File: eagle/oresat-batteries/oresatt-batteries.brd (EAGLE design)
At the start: 94 x 93.5 mm, 22 parts, among them U1 TCAN330

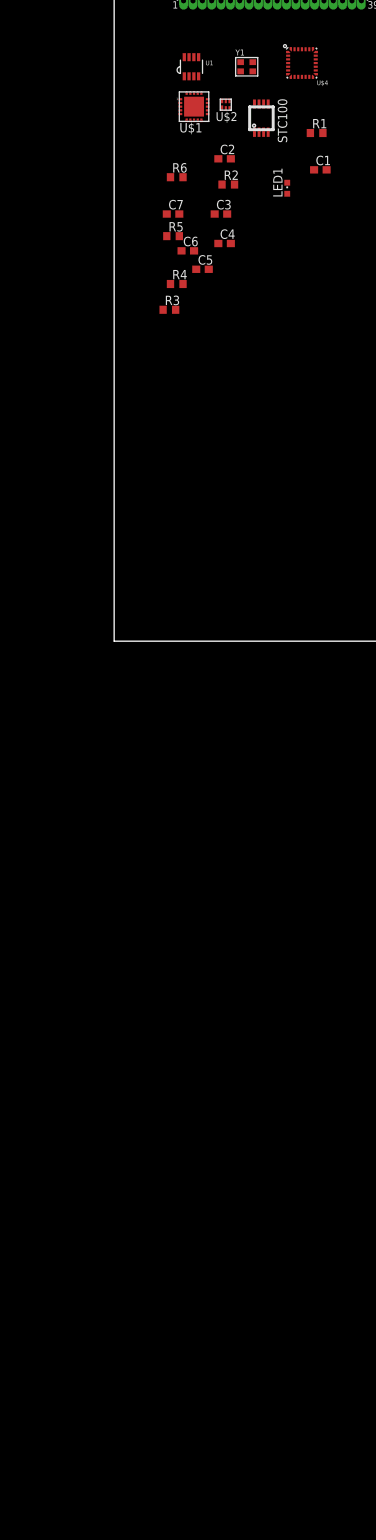
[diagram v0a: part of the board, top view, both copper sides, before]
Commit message: Finished first draft of schematics.
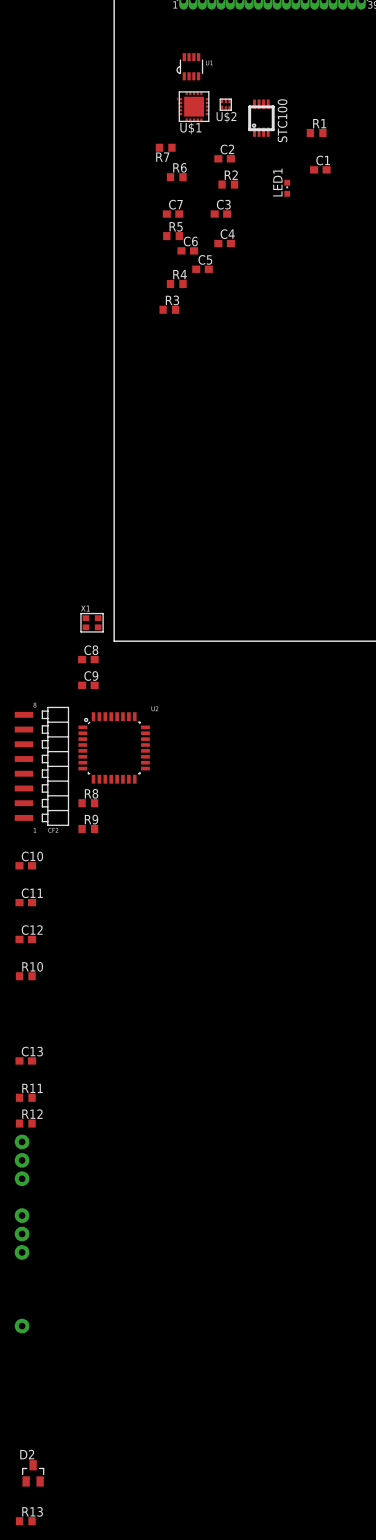
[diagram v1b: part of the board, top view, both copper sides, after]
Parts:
- removed Y1: (no value), low-gain-radio:CRYSTAL_2.5X2
- added C10, C11, C12, C13: 100n, rcl:C0603
- added C8, C9: 20p, rcl:C0603
- added CF2: 2MM-RA-1X8, oresat-batteries:CF-2MM-RA-1X8-PRECIDIP-831
- added D2: BAS40, diode:SOT23
- added R10, R12: 10k, rcl:R0603
- added R11, R7: (no value), rcl:R0603
- added R13: DNP/0, rcl:R0603
- added R8, R9: 4.7k, rcl:R0603
- added U$10, U$11, U$15, U$6, U$7, U$9: TP, oresat-batteries:2MM_TP
- added U2: STM32F042K6, oresat-batteries:QFP32-7X7
- added X1: 16MHz, low-gain-radio:CRYSTAL_2.5X2
- R1: value Sense -> THERMISTER
- R3: value Sense -> .01-.05
- R4: value Sense -> 200k .1%
- U$4: value STM32F042G -> TP; device oresat-batteries:UFQFPN-28 -> oresat-batteries:2MM_TP
- moved U$4 151.3 mm to (-12.5, -68.0)
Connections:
- net N$1 renamed ADP_THR
- net N$10 renamed BQVMIN
- net N$2 renamed LEDNP
- net N$3 renamed ADP_LED
- net N$9 renamed STC_VIN
- removed net N$5: C5.1, CF1.P$3, U$1.6, U$1.7, U$1.8
- removed net N$6: C4.1
- removed net N$8: R3.2
- removed net VCC: U1.3
- removed net VDD: U$4.17
- removed net VDDA: U$4.5
- removed net VDDIO2: U$4.18
- removed net VSS: U$4.16
- new net ADP_CBP: C4.1, U$1.19
- new net BQBAT: C1.1, R7.1, U$2.5
- new net CAN_EN: U1.5, U2.20
- new net CAN_LSTN: U1.8, U2.19
- new net CAN_RX: U1.4, U2.21
- new net CAN_TX: U1.1, U2.22
- new net ISO_S: C3.1, CF1.P$2, U$1.10, U$1.11, U$1.9
- new net N$1: C7.2, R11.1, U$5.7
- new net N$2: R12.2, U2.31
- new net N$3: R10.1, R13.2, U$5.1
- new net N$31: CF2.3, U2.4
- new net OSC_IN: C8.1, U2.2, X1.1
- new net OSC_OUT: C9.1, U2.3, X1.3
- new net SCL: R8.1, U$1.1, U$5.4, U2.29
- new net SDA: R9.1, U$1.17, U$5.3, U2.30
- new net STC_CG: R3.2, U$5.6
- new net STC_IO: R13.1, U2.28
- new net STM_DEBUG: CF2.8, U2.10
- new net SWCLK: CF2.4, U2.24
- new net SWDIO: CF2.5, U2.23
- new net USART2_RX: CF2.7, U2.9
- new net USART2_TX: CF2.6, U2.8
- new net VSOLAR: C5.1, CF1.P$3, R8.2, R9.2, U$1.6, U$1.7, U$1.8
- net GND: now also C10.2, C11.2, C12.2, C13.2, C8.2, C9.2, CF2.1, R12.1, U2.16, U2.32, X1.2, X1.4
- net N$4: now also D2.3; no longer C3.1, U$1.10, U$1.11, U$1.9
- net VBAT+: now also C10.1, C11.1, C12.1, C13.1, CF2.2, D2.1, R11.2, R7.2, U1.3, U2.1, U2.17, U2.5; no longer C1.1, C7.2, U$2.5, U$5.7

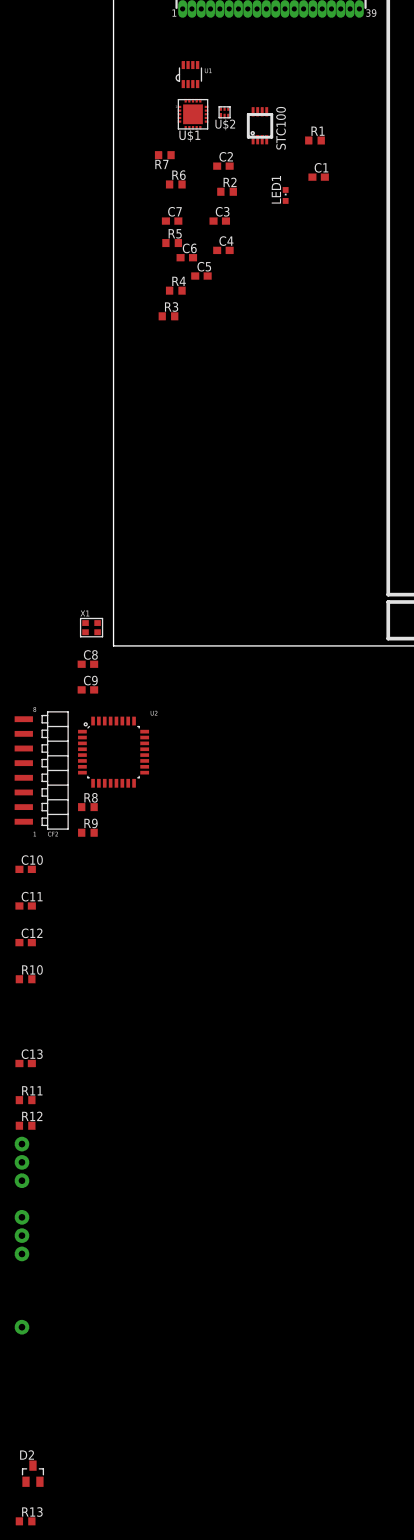
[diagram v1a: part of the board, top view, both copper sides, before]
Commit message: Minor clean up, added debug board, serial marker
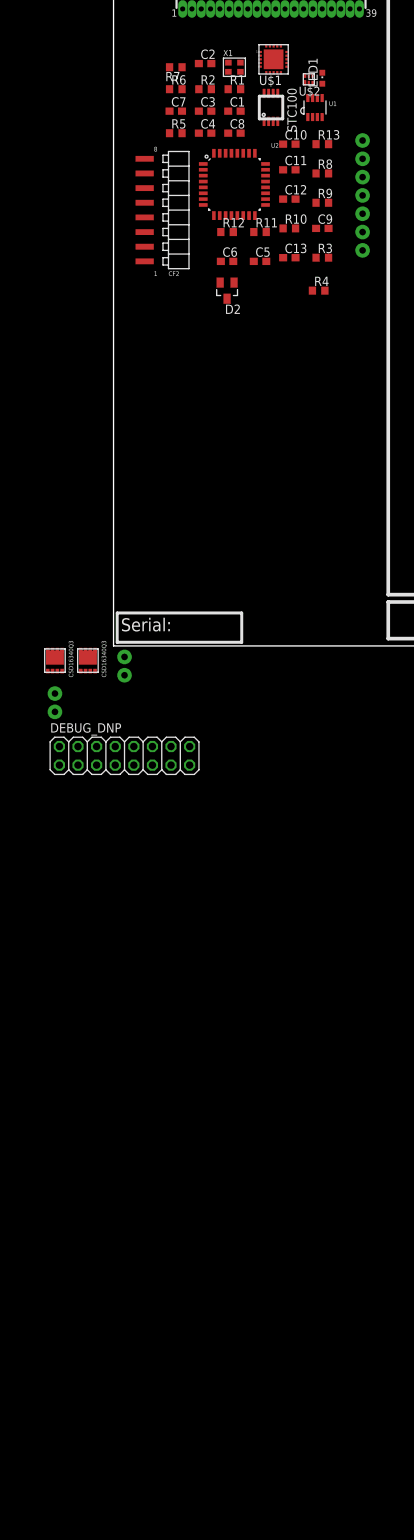
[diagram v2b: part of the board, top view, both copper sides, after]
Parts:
- added DEBUG_DNP: (no value), pinhead:2X08
- added U$12, U$16, U$17, U$8: TP, oresat-batteries:2MM_TP
- added U$13, U$14: CSD16340Q3, oresat-batteries:Q3
- R8, R9: value 4.7k -> 1.6k
- moved R13 192.3 mm to (28.5, 68.5)
- moved D2 163.7 mm to (15.5, 48.5), turned to 180 degrees
- moved U$15 154.2 mm to (34.0, 54.0)
- moved U$10 147.0 mm to (34.0, 59.0)
- moved U$11 147.0 mm to (34.0, 56.5)
- moved U$9 147.0 mm to (34.0, 61.5)
- moved U$4 144.7 mm to (34.0, 69.0)
- moved U$6 144.7 mm to (34.0, 66.5)
- moved U$7 144.7 mm to (34.0, 64.0)
- moved R12 125.1 mm to (15.5, 56.5)
- moved R11 122.7 mm to (20.0, 56.5)
- moved C13 115.7 mm to (24.0, 53.0)
- moved R10 108.6 mm to (24.0, 57.0)
- moved C12 107.7 mm to (24.0, 61.0)
- moved C11 106.8 mm to (24.0, 65.0)
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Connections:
- removed net VBAT+: C10.1, C11.1, C12.1, C13.1, C2.1, CF2.2, D2.1, R11.2, R5.1, R7.2, U$1.12, U$1.13, U$1.14, U$1.4, U1.3, U2.1, U2.17, U2.5
- new net N$10: U$14.P$4, U$2.3
- new net N$11: U$13.P$4, U$2.2
- new net N$5: CF1.P$4, DEBUG_DNP.13, DEBUG_DNP.14, U1.7
- new net N$6: CF1.P$5, DEBUG_DNP.11, DEBUG_DNP.12, U1.6
- new net N$9: U$13.P$5, U$13.P$6, U$13.P$7, U$13.P$8, U$13.P$9, U$14.P$5, U$14.P$6, U$14.P$7, U$14.P$8, U$14.P$9
- new net VBATT+: C10.1, C11.1, C12.1, C13.1, C2.1, CF2.2, D2.1, DEBUG_DNP.1, DEBUG_DNP.2, R11.2, R5.1, R7.2, R8.2, R9.2, U$1.12, U$1.13, U$1.14, U$1.4, U1.3, U2.1, U2.17, U2.5
- net GND: now also DEBUG_DNP.15, DEBUG_DNP.16, U$13.P$1, U$13.P$2, U$13.P$3
- net SCL: now also R9.1; no longer R8.1
- net SDA: now also R8.1; no longer R9.1
- net STC_CG: now also U$14.P$1, U$14.P$2, U$14.P$3
- net USART2_RX: now also DEBUG_DNP.5, DEBUG_DNP.6
- net USART2_TX: now also DEBUG_DNP.3, DEBUG_DNP.4
- net VSOLAR: now also DEBUG_DNP.7, DEBUG_DNP.8; no longer R8.2, R9.2
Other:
- board text added: "Serial:"

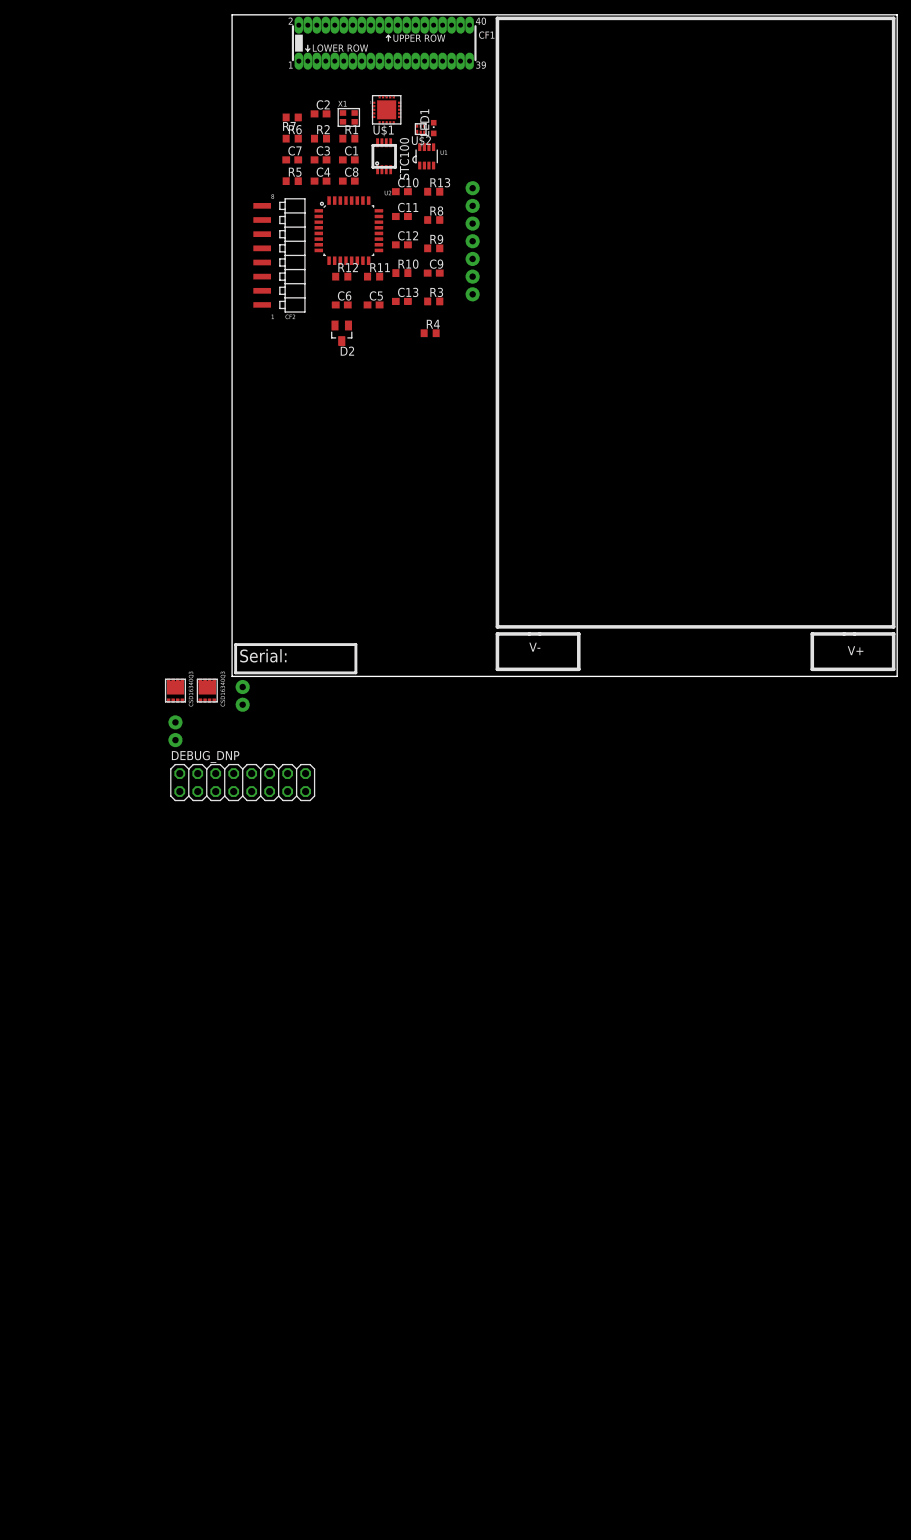
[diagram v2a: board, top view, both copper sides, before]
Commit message: Added, resistive heater, half of shutdown circuitry, connected DIG_IOx and SYS_EN pins.
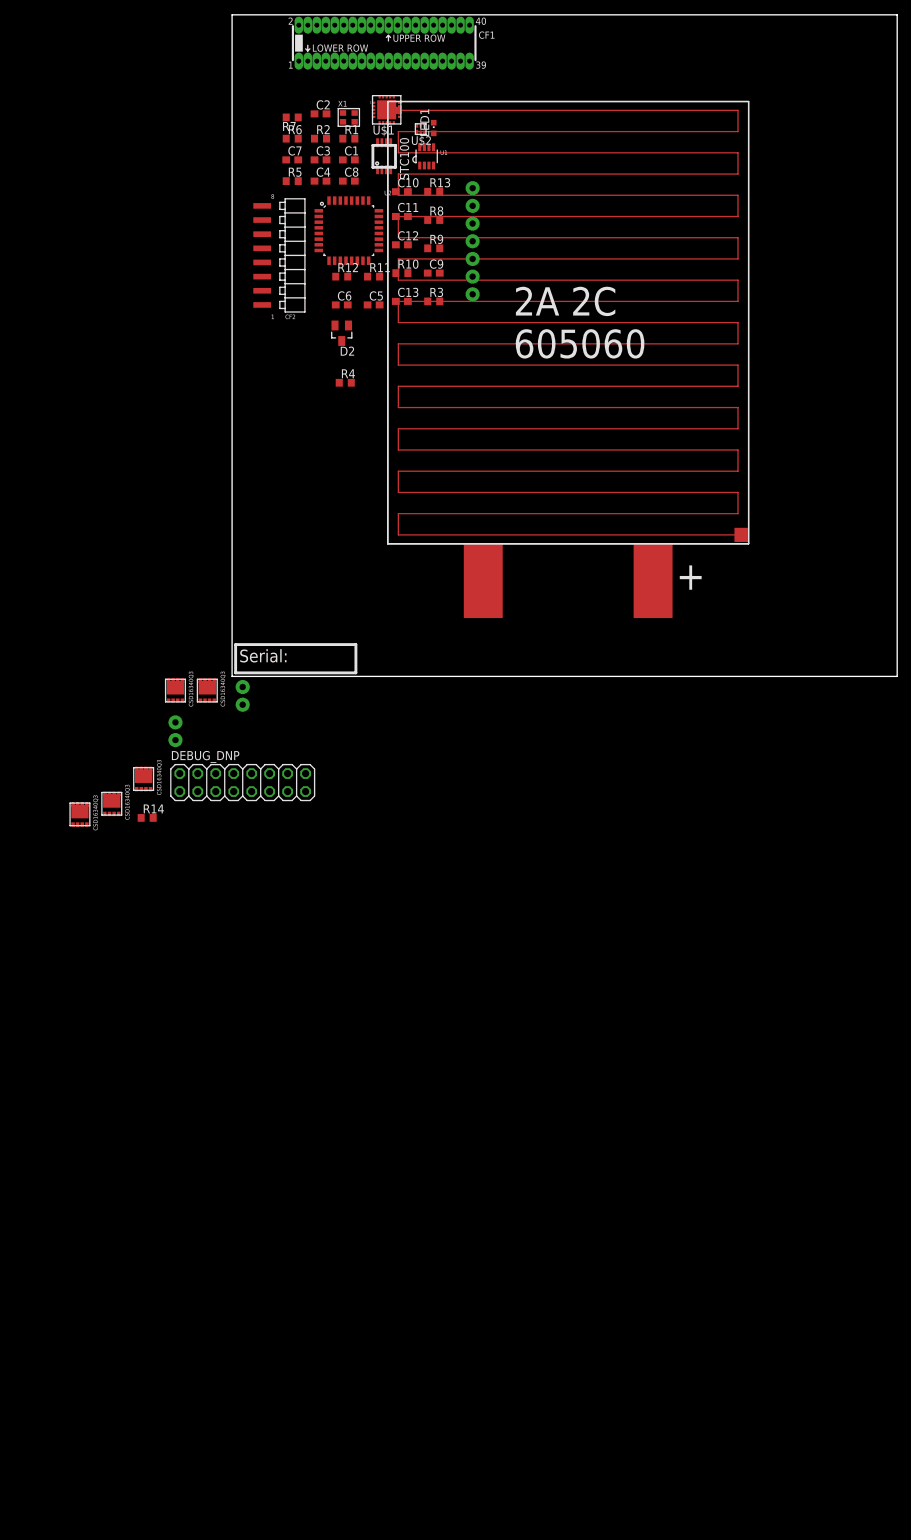
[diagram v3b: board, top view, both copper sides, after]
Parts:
- added R14: 100k, rcl:R0603
- added U$18, U$19, U$20: CSD16340Q3, oresat-batteries:Q3
- added U$21: 4.19, oresat-batteries:RES_HEATER
- U$3: value 1.5AHBATT -> 2AHBATT; device oresat-batteries:1.5AH -> oresat-batteries:2AH_605060
- moved U$3 18.0 mm to (47.5, 50.0)
- moved R4 13.9 mm to (16.0, 41.5)
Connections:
- net N$11 renamed COUT
- net N$9 renamed BETSHUT
- new net BATTHICUT: U$19.P$5, U$19.P$6, U$19.P$7, U$19.P$8, U$19.P$9, U$3.POS
- new net BQKILL: R6.2, U$18.P$5, U$18.P$6, U$18.P$7, U$18.P$8, U$18.P$9, U$2.4
- new net DOUT: CF1.P$40, R14.1, U$14.P$4, U$18.P$4, U$19.P$4, U$2.3
- new net N$11: U$1.2, U2.27
- new net N$13: U$20.P$1, U$20.P$2, U$20.P$3, U$21.V+
- new net N$14: U$20.P$4, U2.7
- new net N$8: U$1.16, U2.14
- new net N$9: U$1.5, U2.15
- net GND: now also U$18.P$1, U$18.P$2, U$18.P$3, U$21.V-; no longer R6.2, U$2.4
- net N$10: now also U$1.3, U2.26; no longer U$14.P$4, U$2.3
- net STC_CG: now also U$3.NEG
- net STC_VIN: now also R5.1; no longer R5.2
- net VBATT+: now also R14.2, R5.2, U$19.P$1, U$19.P$2, U$19.P$3, U$20.P$5, U$20.P$6, U$20.P$7, U$20.P$8, U$20.P$9; no longer R5.1

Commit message: Fixed Shutdown Circuit, Added more ground pins, cleaned up schematic
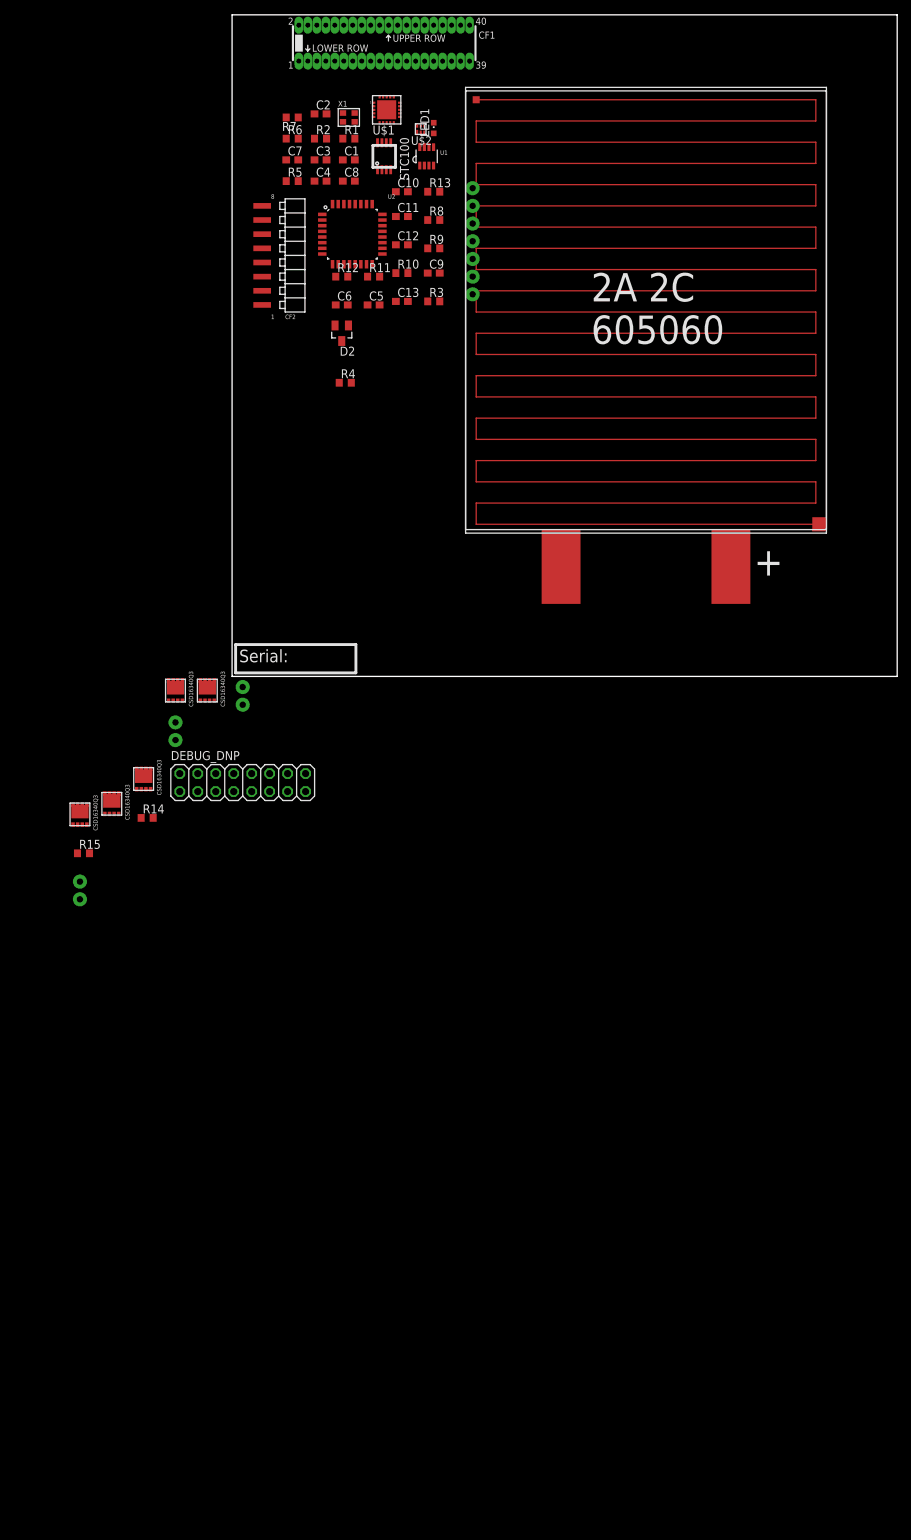
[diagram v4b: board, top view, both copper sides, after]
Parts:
- added R15: 100k, rcl:R0603
- added U$22, U$23: TP, oresat-batteries:2MM_TP
- moved U$3 11.2 mm to (58.5, 52.0)
- moved U$21 11.1 mm to (58.5, 51.5)
- moved U2 0.71 mm to (17.0, 62.5)
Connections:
- new net SHORTBAR: CF1.P$40, R14.1, R15.1, U$18.P$4, U$19.P$4
- net DOUT: no longer CF1.P$40, R14.1, U$18.P$4, U$19.P$4
- net GND: now also R15.2

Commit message: Added TP and nominal V for shutoff
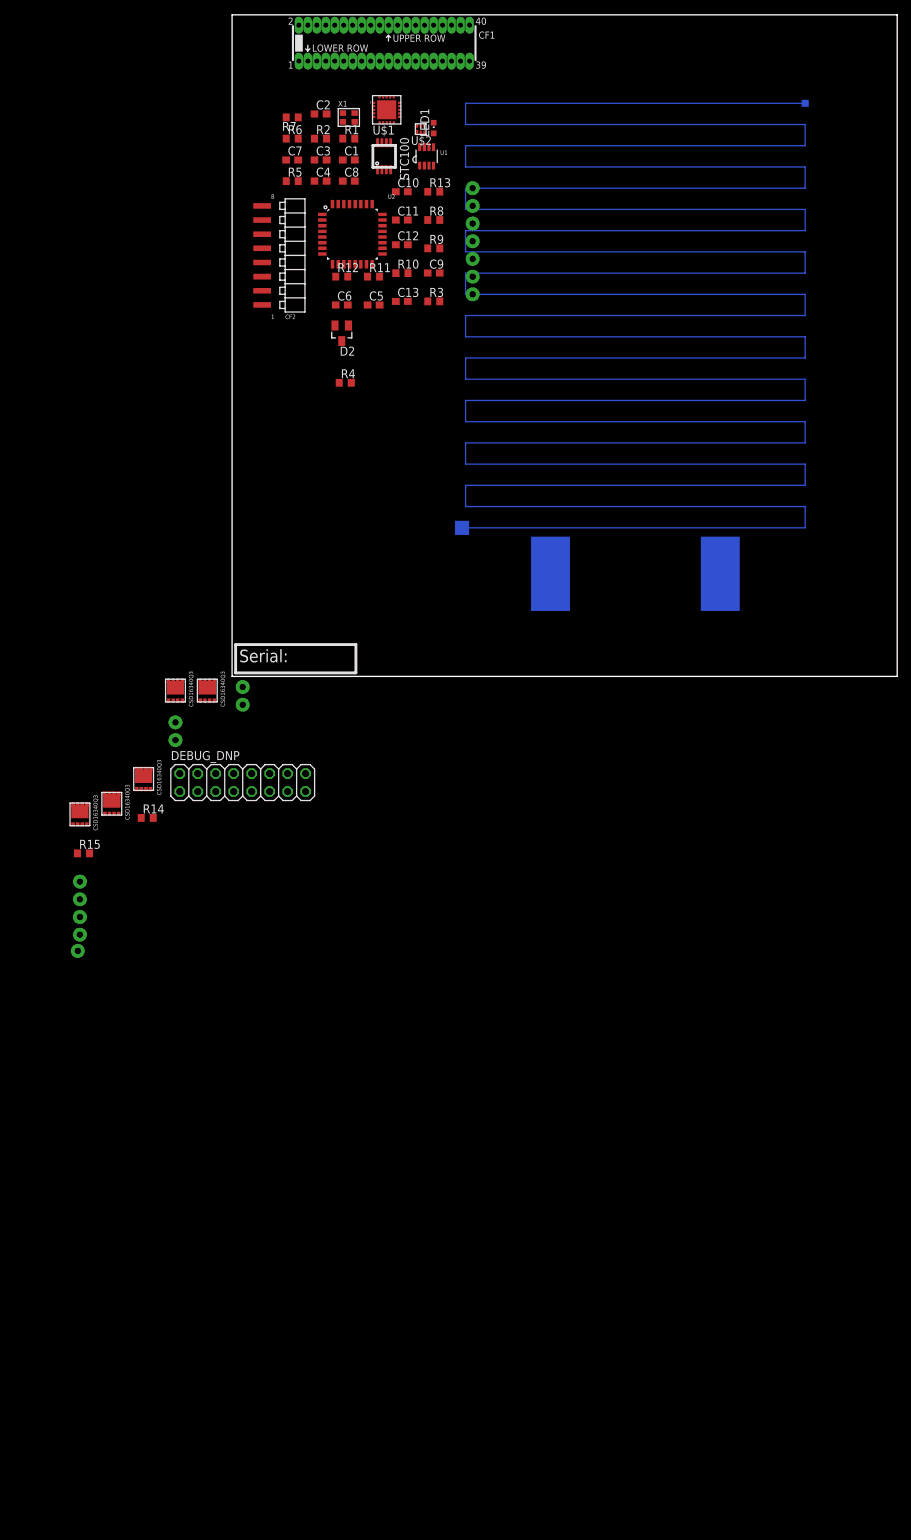
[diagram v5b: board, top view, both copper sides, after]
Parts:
- added U$24, U$25, U$26: TP, oresat-batteries:2MM_TP
- R14: value 100k -> 20k
- R15: value 100k -> 200k
- moved U$3 1.80 mm to (57.0, 51.0), flipped to the bottom
- moved U$21 1.58 mm to (57.0, 51.0), flipped to the bottom
- moved C11 0.50 mm to (24.0, 64.5)
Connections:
- net SHORTBAR: now also CF1.P$6; no longer CF1.P$40
